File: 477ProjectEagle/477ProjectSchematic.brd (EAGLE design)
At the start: 101.6 x 127 mm, 77 parts, among them J1 POWER_JACK_BAT, J2 POWER_JACK_12VOUT, J3 RJ11-6PTH, Q1 AO4419, X1 22-23-2051, X10 MOTORS

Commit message: Fixed Schematic to include cap for internal reg
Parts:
- added U$3: 10uF, MinotaurParts:C1206
- U$23, U$24, U$25, U$40, U$43, U$44, U$6: value 10uF -> 0.1uF
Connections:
- removed net N$98: SV7.8, U$1.57
- net +3V3: now also SV7.8, U$1.57
- net GND: now also U$3.2
- net N$67: now also U$3.1
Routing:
- net +3V3: track 250.4 -> 266.8 mm
- net N$98: track 9.55 -> 0.00 mm
- net N$67: track 6.89 -> 14.2 mm, vias 0 -> 1
- net GND: track 916.4 -> 920.7 mm
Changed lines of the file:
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@@
 <element name="CIN7" library="MinotaurParts" package="C1210" value="10uF" x="70.9168" y="15.8496"/>
 <element name="L1_7" library="MinotaurParts" package="SRR1210" value="12uH" x="60.1218" y="21.5646" rot="R270"/>
-<element name="U$23" library="MinotaurParts" package="C1206" value="10uF" x="30.3276" y="79.4004" rot="MR180"/>
-<element name="U$24" library="MinotaurParts" package="C1206" value="10uF" x="30.3784" y="66.6496" rot="MR180"/>
-<element name="U$25" library="MinotaurParts" package="C1206" value="10uF" x="23.0632" y="73.914" rot="MR90"/>
-<element name="U$40" library="MinotaurParts" package="C1206" value="10uF" x="73.7108" y="98.044" rot="MR180"/>
-<element name="U$43" library="MinotaurParts" package="C1206" value="10uF" x="60.6552" y="88.138" rot="R90"/>
-<element name="U$44" library="MinotaurParts" package="C1206" value="10uF" x="54.1528" y="88.1888" rot="R90"/>
+<element name="U$23" library="MinotaurParts" package="C1206" value="0.1uF" x="30.3276" y="79.4004" rot="MR180"/>
+<element name="U$24" library="MinotaurParts" package="C1206" value="0.1uF" x="30.3784" y="66.6496" rot="MR180"/>
+<element name="U$25" library="MinotaurParts" package="C1206" value="0.1uF" x="23.0632" y="73.914" rot="MR90"/>
+<element name="U$40" library="MinotaurParts" package="C1206" value="0.1uF" x="73.7108" y="98.044" rot="MR180"/>
+<element name="U$43" library="MinotaurParts" package="C1206" value="0.1uF" x="60.6552" y="88.138" rot="R90"/>
+<element name="U$44" library="MinotaurParts" package="C1206" value="0.1uF" x="54.1528" y="88.1888" rot="R90"/>
 <element name="U$45" library="MinotaurParts" package="C1206" value="10uF" x="14.5796" y="91.186" rot="R90"/>
 <element name="U$46" library="MinotaurParts" package="C1206" value="10uF" x="14.6304" y="97.1804" rot="R90"/>
@@
 <attribute name="OC_FARNELL" value="unknown" x="30.1244" y="59.8424" size="1.778" layer="27" rot="R180" display="off"/>
 </element>
-<element name="U$6" library="MinotaurParts" package="C1206" value="10uF" x="29.2608" y="73.9648" rot="MR270"/>
+<element name="U$6" library="MinotaurParts" package="C1206" value="0.1uF" x="29.2608" y="73.9648" rot="MR270"/>
 <element name="D1" library="diode" package="DO-214AC" value="" x="36.2204" y="4.5212"/>
 <element name="D2" library="diode" package="DO-214AC" value="" x="30.226" y="10.7696" rot="R180"/>
@@
 <element name="POWER" library="led" package="1206" value="" x="73.6092" y="121.3612"/>
 <element name="RLED2" library="MinotaurParts" package="R1206" value="1k" x="64.4652" y="117.5512"/>
+<element name="U$3" library="MinotaurParts" package="C1206" value="10uF" x="35.3568" y="72.5424" rot="MR270"/>
 </elements>
 <signals>
@@
 <via x="31.6992" y="70.4596" extent="1-16" drill="0.6"/>
 <wire x1="5.2832" y1="114.6048" x2="5.2324" y2="114.554" width="0.3048" layer="16"/>
+<contactref element="U$3" pad="2"/>
+<wire x1="31.75" y1="70.5104" x2="31.6992" y2="70.4596" width="0.4064" layer="16"/>
+<wire x1="35.3568" y1="71.1424" x2="35.176" y2="71.1424" width="0.4064" layer="16"/>
+<wire x1="35.176" y1="71.1424" x2="34.1376" y2="70.104" width="0.4064" layer="16"/>
+<wire x1="34.1376" y1="70.104" x2="32.0548" y2="70.104" width="0.4064" layer="16"/>
+<wire x1="32.0548" y1="70.104" x2="31.6992" y2="70.4596" width="0.4064" layer="16"/>
+<wire x1="33.0176" y1="17.2974" x2="33.0176" y2="27.4574" width="0" layer="19" extent="1-1"/>
+<wire x1="33.0176" y1="16.0274" x2="33.0176" y2="17.2974" width="0" layer="19" extent="1-1"/>
+<wire x1="65.2272" y1="5.4864" x2="65.2018" y2="5.8166" width="0" layer="19" extent="1-1"/>
+<wire x1="20.0176" y1="17.2974" x2="20.0176" y2="16.0274" width="0" layer="19" extent="1-1"/>
+<wire x1="20.0176" y1="26.1874" x2="20.0176" y2="17.2974" width="0" layer="19" extent="1-1"/>
+<wire x1="20.0176" y1="27.4574" x2="20.0176" y2="26.1874" width="0" layer="19" extent="1-1"/>
 </signal>
 <signal name="N$16">
@@
 <wire x1="25.908" y1="72.5424" x2="24.8158" y2="72.5424" width="0.3048" layer="1"/>
 <wire x1="27.94" y1="75.8952" x2="29.2608" y2="74.5744" width="0.6096" layer="1"/>
-<wire x1="29.2608" y1="74.5744" x2="29.2608" y2="70.3072" width="0.6096" layer="1"/>
+<wire x1="29.2608" y1="74.5744" x2="29.2608" y2="73.5584" width="0.6096" layer="1"/>
+<wire x1="29.2608" y1="73.5584" x2="29.2608" y2="70.3072" width="0.6096" layer="1"/>
 <wire x1="29.2608" y1="70.3072" x2="29.21" y2="70.2564" width="0.6096" layer="1"/>
 <wire x1="29.21" y1="70.2564" x2="29.21" y2="69.2912" width="0.3048" layer="1"/>
@@
 <wire x1="38.2016" y1="112.1664" x2="35.5346" y2="112.1664" width="0.4064" layer="16"/>
 <wire x1="35.5346" y1="112.1664" x2="35.433" y2="112.268" width="0.4064" layer="16"/>
+<contactref element="SV7" pad="8"/>
+<contactref element="U$1" pad="57"/>
+<wire x1="36.0426" y1="73.5584" x2="43.942" y2="73.5584" width="0.3048" layer="1"/>
+<wire x1="43.942" y1="73.5584" x2="45.1104" y2="74.7268" width="0.3048" layer="1"/>
+<wire x1="36.0426" y1="73.5584" x2="29.2608" y2="73.5584" width="0.3048" layer="1"/>
 </signal>
 <signal name="+12V">
@@
 <wire x1="36.0426" y1="73.0504" x2="41.7068" y2="73.0504" width="0.3048" layer="1"/>
 <wire x1="41.7068" y1="73.0504" x2="42.5704" y2="72.1868" width="0.3048" layer="1"/>
+<contactref element="U$3" pad="1"/>
+<wire x1="36.0426" y1="73.0504" x2="34.8488" y2="73.0504" width="0.3048" layer="1"/>
+<wire x1="34.8488" y1="73.0504" x2="33.7312" y2="71.9328" width="0.3048" layer="1"/>
+<via x="33.7312" y="71.9328" extent="1-16" drill="0.6"/>
+<wire x1="33.7312" y1="71.9328" x2="33.528" y2="71.9328" width="0.3048" layer="16"/>
+<wire x1="33.528" y1="71.9328" x2="32.9184" y2="72.5424" width="0.3048" layer="16"/>
+<wire x1="32.9184" y1="72.5424" x2="32.9184" y2="73.3552" width="0.3048" layer="16"/>
+<wire x1="32.9184" y1="73.3552" x2="33.528" y2="73.9648" width="0.3048" layer="16"/>
+<wire x1="33.528" y1="73.9648" x2="35.3344" y2="73.9648" width="0.3048" layer="16"/>
+<wire x1="35.3344" y1="73.9648" x2="35.3568" y2="73.9424" width="0.3048" layer="16"/>
 </signal>
 <signal name="N$94">
@@
 <wire x1="42.5196" y1="77.216" x2="42.5704" y2="77.2668" width="0.3048" layer="1"/>
 </signal>
-<signal name="N$98">
-<contactref element="SV7" pad="8"/>
-<contactref element="U$1" pad="57"/>
-<wire x1="36.0426" y1="73.5584" x2="43.942" y2="73.5584" width="0.3048" layer="1"/>
-<wire x1="43.942" y1="73.5584" x2="45.1104" y2="74.7268" width="0.3048" layer="1"/>
-</signal>
 <signal name="N$96">

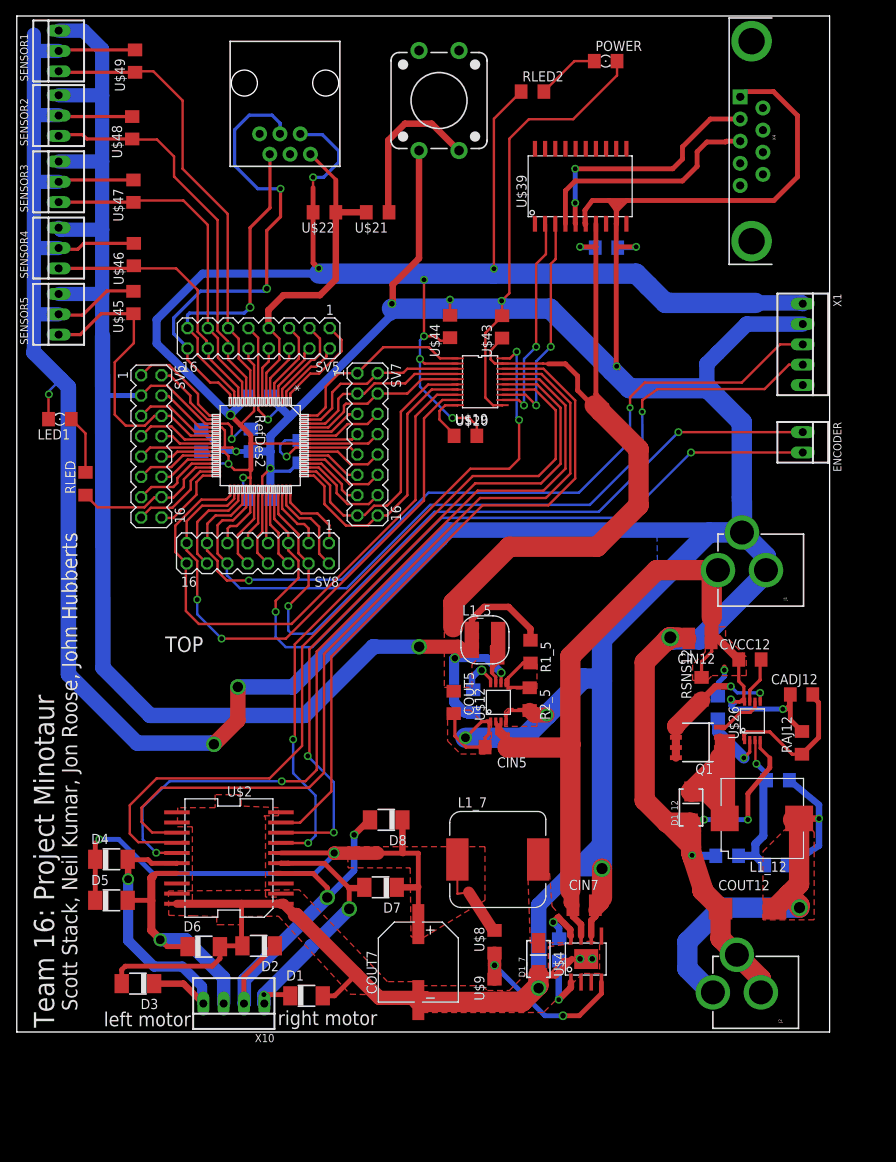
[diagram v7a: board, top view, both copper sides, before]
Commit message: Worked on PIC software
Implemented a circular send and receive buffer for the UART. Tested it
and got it working. Fixed the H-Bridge package. Wrote a txt document
with all the things that need to be fixed on the PCB.
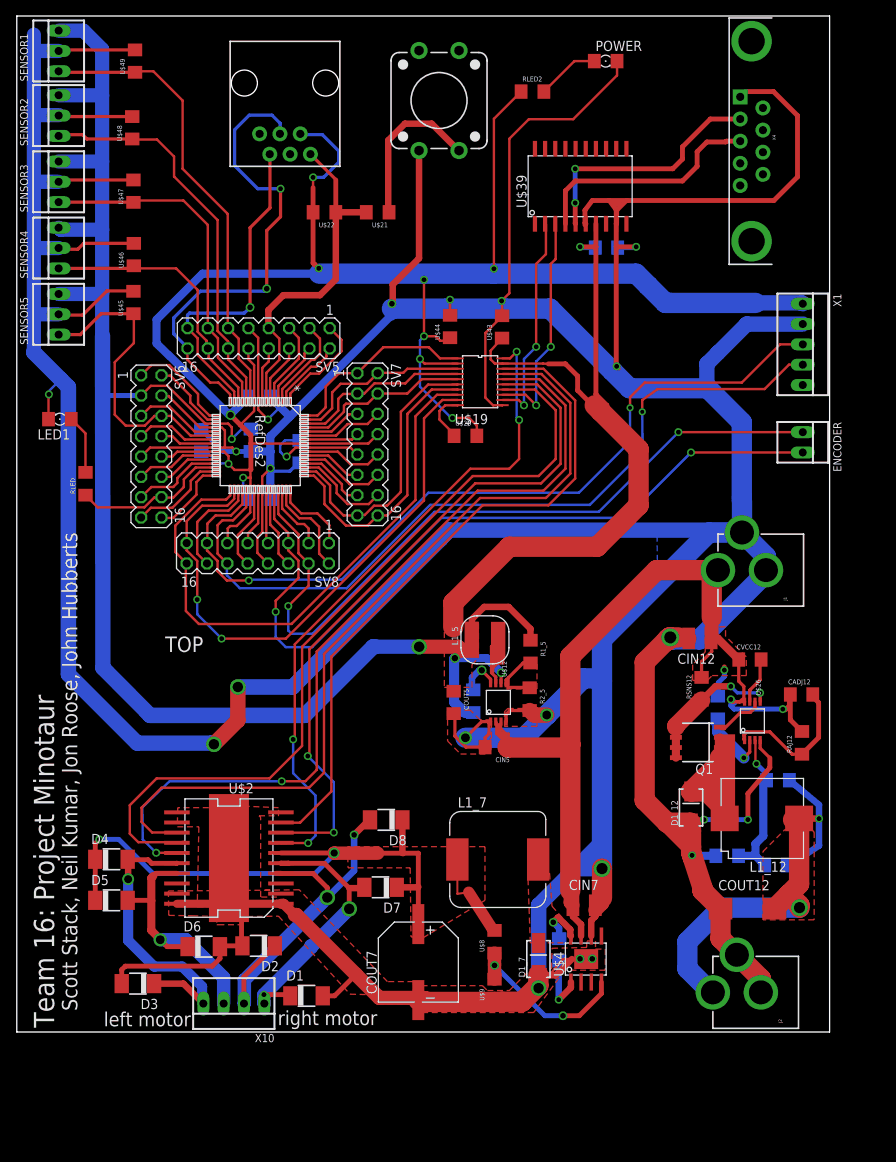
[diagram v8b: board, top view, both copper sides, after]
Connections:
- net GND: now also U$2.GNDPAD
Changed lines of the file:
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@@
 <setting verticaltext="up"/>
 </settings>
-<grid distance="8" unitdist="mil" unit="mil" style="lines" multiple="1" display="yes" altdistance="0.025" altunitdist="inch" altunit="inch"/>
+<grid distance="2" unitdist="mil" unit="mil" style="lines" multiple="1" display="yes" altdistance="0.025" altunitdist="inch" altunit="inch"/>
 <layers>
 <layer number="1" name="Top" color="4" fill="1" visible="yes" active="yes"/>
@@
 <wire x1="73.152" y1="16.0752" x2="72.3168" y2="15.24" width="1.778" layer="1"/>
 <polygon width="0.3048" layer="1" thermals="no">
-<vertex x="71.882" y="11.3792"/>
-<vertex x="72.8472" y="10.9728"/>
-<vertex x="72.8472" y="7.3152"/>
-<vertex x="70.7136" y="7.3152"/>
-<vertex x="65.8368" y="2.4384"/>
+<vertex x="71.2724" y="11.3792"/>
+<vertex x="72.3392" y="11.3792"/>
+<vertex x="72.3392" y="10.3632"/>
+<vertex x="73.5584" y="10.3632"/>
+<vertex x="73.5584" y="7.7216"/>
+<vertex x="68.4784" y="7.7216"/>
+<vertex x="64.6176" y="2.4384"/>
 <vertex x="50.5968" y="2.4384"/>
 <vertex x="50.5968" y="5.7912"/>
@@
 <vertex x="61.5696" y="5.1816"/>
 <vertex x="64.3128" y="7.9248"/>
-<vertex x="66.4464" y="7.9248"/>
-<vertex x="66.4464" y="10.668"/>
-<vertex x="71.4248" y="11.3284"/>
+<vertex x="66.8528" y="7.9248"/>
+<vertex x="66.9036" y="10.4648"/>
+<vertex x="71.2216" y="10.5664"/>
 </polygon>
 <wire x1="71.1708" y1="9.1186" x2="68.2498" y2="9.1186" width="0.3048" layer="1"/>
@@
 <wire x1="50.64959375" y1="4.2672" x2="51.11340625" y2="3.8033875" width="1.778" layer="1"/>
 <wire x1="33.0176" y1="16.0274" x2="28.0924" y2="16.0274" width="1.016" layer="1"/>
-<polygon width="0.3048" layer="1">
+<polygon width="0.3048" layer="1" thermals="no">
 <vertex x="32.7152" y="27.0256"/>
 <vertex x="32.7152" y="28.0416"/>
 <vertex x="28.0416" y="28.2448"/>
-<vertex x="28.0416" y="29.6672"/>
-<vertex x="24.7904" y="29.6672"/>
-<vertex x="24.7904" y="28.0416"/>
+<vertex x="27.8384" y="28.2448"/>
+<vertex x="25.1968" y="28.0416"/>
 <vertex x="20.1168" y="28.0416"/>
 <vertex x="20.066" y="25.654"/>
-<vertex x="21.9456" y="25.654"/>
-<vertex x="21.9456" y="15.8496"/>
+<vertex x="22.7584" y="25.654"/>
+<vertex x="22.5552" y="15.6464"/>
 <vertex x="32.512" y="15.8496"/>
 <vertex x="32.512" y="16.8656"/>
-<vertex x="31.0896" y="16.8656"/>
-<vertex x="31.0896" y="26.8224"/>
-<vertex x="30.8864" y="27.0256"/>
+<vertex x="30.48" y="16.8656"/>
+<vertex x="30.48" y="26.8224"/>
+<vertex x="30.2768" y="27.0256"/>
 </polygon>
 <wire x1="28.0924" y1="16.0274" x2="20.0176" y2="16.0274" width="1.016" layer="1"/>
@@
 <wire x1="34.1376" y1="70.104" x2="32.0548" y2="70.104" width="0.4064" layer="16"/>
 <wire x1="32.0548" y1="70.104" x2="31.6992" y2="70.4596" width="0.4064" layer="16"/>
-<wire x1="33.0176" y1="17.2974" x2="33.0176" y2="27.4574" width="0" layer="19" extent="1-1"/>
-<wire x1="33.0176" y1="16.0274" x2="33.0176" y2="17.2974" width="0" layer="19" extent="1-1"/>
-<wire x1="65.2272" y1="5.4864" x2="65.2018" y2="5.8166" width="0" layer="19" extent="1-1"/>
-<wire x1="20.0176" y1="17.2974" x2="20.0176" y2="16.0274" width="0" layer="19" extent="1-1"/>
-<wire x1="20.0176" y1="26.1874" x2="20.0176" y2="17.2974" width="0" layer="19" extent="1-1"/>
-<wire x1="20.0176" y1="27.4574" x2="20.0176" y2="26.1874" width="0" layer="19" extent="1-1"/>
+<contactref element="U$2" pad="GNDPAD"/>
 </signal>
 <signal name="N$16">
